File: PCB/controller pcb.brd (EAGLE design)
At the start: 84 x 86.5 mm, 43 parts, among them IC1 MAX481CSA, IC2 MAX481CSA, IC3 STM32F103C8T, U1 TPS62177.DQC, X2 2510-, X4 NC3FAH2, X5 NC3FAH2-0, X7 MINI-USB_4P-85-32004-40X

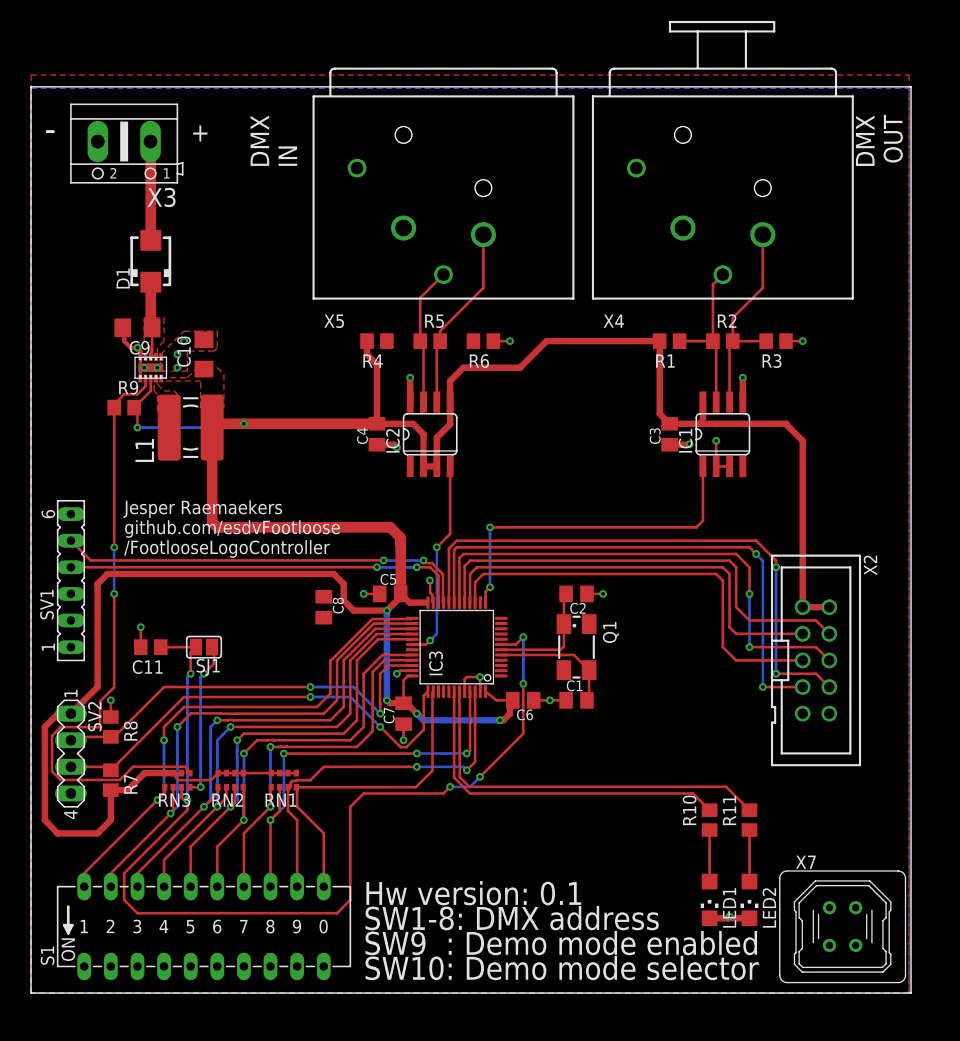
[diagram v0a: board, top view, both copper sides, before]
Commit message: Minor changes to fron PCB. changed positioning of segments and buttons
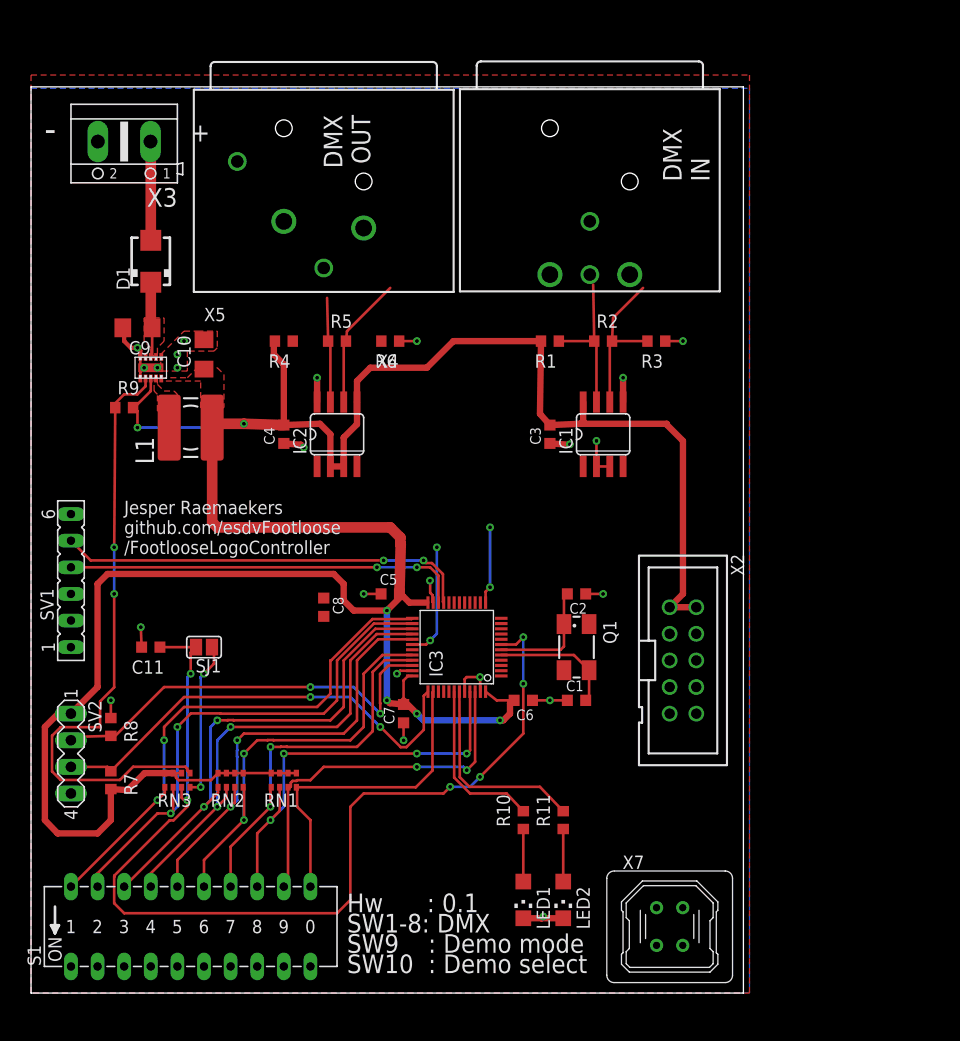
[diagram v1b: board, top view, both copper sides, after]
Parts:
- C1, C2, C3, C4, C5, C6, C7, C8: device rcl:C0805K -> rcl:C0603K
- C11: device rcl:C0805 -> rcl:C0603K
- R1, R10, R11, R2, R3, R4, R5, R6, R7, R8, R9: device rcl:R0805 -> rcl:R0603
- X4: value NC3FAH2 -> NC3MBH; device con-neutrik_ag:NC3FAH2 -> con-neutrik_ag:NC3MBH
- moved LED2 17.8 mm to (50.8, 8.89)
- moved R11 17.8 mm to (50.8, 16.5)
- moved LED1 17.8 mm to (47.0, 8.89)
- moved R10 17.8 mm to (47.0, 16.5)
- moved X7 16.5 mm to (61.0, 6.35)
- moved X4 13.3 mm to (53.3, 68.6)
- moved X2 12.7 mm to (62.2, 31.8)
- moved X5 11.4 mm to (27.9, 73.0)
- moved IC1 11.4 mm to (54.6, 53.3)
- moved R2 11.4 mm to (54.6, 62.2)
- moved R3 11.4 mm to (59.7, 62.2)
- moved C3 11.4 mm to (49.5, 53.3)
- moved R1 11.4 mm to (49.5, 62.2)
- moved C4 8.89 mm to (24.1, 53.3)
- moved R4 8.89 mm to (24.1, 62.2)
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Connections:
- removed net FP_CS1: IC3.18, X2.6
- removed net FP_CS2: IC3.19, X2.7
- removed net FP_CS3: IC3.20, X2.8
- removed net FP_MISO: IC3.16, X2.3
- removed net FP_MOSI: IC3.17, X2.4
- removed net FP_SCK: IC3.15, X2.5
- removed net VDDA: IC3.9
- removed net VSSA: IC3.8
- new net FP_!RESET: X2.5
- new net FP_SCL: X2.4
- new net FP_SDA: X2.3
- new net FP_SYNC: X2.6
- new net FP_TOUCH1: X2.7
- new net FP_TOUCH2: X2.8
- net +3V3: now also C8.1, IC3.9
- net GND: now also C8.2, IC3.8, X4.2; no longer X4.1
- net N$6: now also X4.1; no longer X4.2
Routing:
- net FP_CS3: track 53.9 -> 0.00 mm, vias 2 -> 0
- net FP_CS2: track 51.0 -> 0.00 mm, vias 2 -> 0
- net FP_CS1: track 48.4 -> 0.00 mm, vias 2 -> 0
- net FP_MOSI: track 43.6 -> 0.00 mm
- net FP_SCK: track 40.7 -> 0.00 mm
- net FP_MISO: track 40.4 -> 0.00 mm
- net DMX_IN: track 33.1 -> 7.36 mm
- net N$12: track 37.1 -> 19.4 mm
- net N$13: track 33.9 -> 16.2 mm
- net +3V3: track 274.7 -> 265.0 mm
- net DMX_OUT: track 19.3 -> 11.1 mm
- net N$7: track 17.8 -> 12.7 mm
- net N$6: track 20.5 -> 15.5 mm
- net N$8: track 13.2 -> 10.0 mm
- net !RST: track 94.5 -> 96.3 mm
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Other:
- board size 84 x 86.5 mm -> 68 x 86.5 mm
- board text added: "Hw : 0.1 SW1-8: DMX SW9 : Demo mode SW10 : Demo select"
- board text removed: "Hw version: 0.1 SW1-8: DMX address SW9 : Demo mode enabled SW10: Demo mode selector"

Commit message: pending changes...
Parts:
- added C12: (no value), rcl:C0603K
- added IC4: MAX481CSA, maxim:SO08
- added R12, R13, R14: (no value), rcl:R0603
- added X1: NC3FAH2-0, con-neutrik_ag:NC3FAH2-0
- moved X5 64.9 mm to (53.3, 13.3), turned to 180 degrees
- moved R4 50.3 mm to (61.0, 27.9), turned to 90 degrees
- moved R5 49.1 mm to (61.0, 24.8), turned to 270 degrees
- moved R6 48.6 mm to (61.0, 21.6), turned to 90 degrees
- moved C4 44.0 mm to (54.0, 21.0), turned to 0 degrees
- moved IC2 37.8 mm to (54.0, 24.8), turned to 270 degrees
- moved X7 27.4 mm to (80.6, 25.4)
- moved LED1 13.7 mm to (34.3, 3.81)
- moved LED2 13.7 mm to (38.1, 3.81)
- moved R10 12.8 mm to (34.3, 15.2)
- moved R11 12.8 mm to (38.1, 15.2)
- moved X2 8.28 mm to (61.6, 40.0)
- moved C1 2.84 mm to (53.3, 30.5)
- moved C2 2.84 mm to (53.3, 40.6)
- moved C5 2.84 mm to (35.6, 40.6)
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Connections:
- new net N$11: IC4.7, R12.1, R13.1, X1.3
- new net N$2: IC4.6, R13.2, R14.2, X1.2
- net +3V3: now also C12.1, IC1.5, IC4.2, IC4.3, IC4.5, R12.2; no longer IC1.8
- net DMX_IN: now also IC4.4
- net GND: now also C12.2, IC1.8, IC4.8, R14.1, X1.1, X1.G; no longer IC1.5
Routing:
- net +3V3: track 265.0 -> 305.1 mm, vias 6 -> 8
- net DMX_IN: track 7.36 -> 37.8 mm, vias 2 -> 0
- net N$2: track 0.00 -> 21.5 mm
- net N$7: track 12.7 -> 30.1 mm
- net N$11: track 0.00 -> 17.3 mm
- net DMX_OUT: track 11.1 -> 27.5 mm
- net GND: track 46.0 -> 30.1 mm, vias 23 -> 17
- net N$8: track 10.0 -> 24.5 mm
- net !RST: track 96.3 -> 105.9 mm
- net SWCLK: track 43.3 -> 51.5 mm
- net SWDIO: track 39.9 -> 47.3 mm
- net DIPSW1: track 50.3 -> 57.3 mm
- net N$14: track 15.0 -> 21.9 mm
- net DIPSW5: track 42.4 -> 48.2 mm
- net DIPSW3: track 46.8 -> 52.4 mm
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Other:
- board text added: "1-9: DMX 10 : Test"
- board text removed: "Hw : 0.1 SW1-8: DMX SW9 : Demo mode SW10 : Demo select"

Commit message: Updated to STM32f303
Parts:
- removed IC3: STM32F103C8T, micro-stm:LQFP48
- removed X7: MINI-USB_4P-85-32004-40X, con-cypressindustries:85-32004-40X
- added U$1: STM32F303CCLQFP48, comp:LQFP48
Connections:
- removed net FP_!RESET: X2.5
- removed net N$15: IC3.39
- removed net VBAT: IC3.1
- net !RST: now also U$1.7, X2.5; no longer IC3.7
- net +3V3: now also U$1.24, U$1.36, U$1.48, U$1.9; no longer IC3.24, IC3.36, IC3.48, IC3.9
- net DEBUG_RX: now also U$1.22; no longer IC3.22
- net DEBUG_TX: now also U$1.21; no longer IC3.21
- net DIPSW1: now also U$1.25; no longer IC3.25
- net DIPSW10: now also U$1.38; no longer IC3.38
- net DIPSW2: now also U$1.26; no longer IC3.26
- net DIPSW3: now also U$1.27; no longer IC3.27
- net DIPSW4: now also U$1.28; no longer IC3.28
- net DIPSW5: now also U$1.29; no longer IC3.29
- net DIPSW6: now also U$1.32; no longer IC3.32
- net DIPSW7: now also U$1.33; no longer IC3.33
- net DIPSW8: now also U$1.45; no longer IC3.45
- net DIPSW9: now also U$1.46; no longer IC3.46
- net DMX_IN: now also U$1.13; no longer IC3.13
- net DMX_OUT: now also U$1.30; no longer IC3.30
- net FP_SCL: now also U$1.42
- net FP_SDA: now also U$1.43
- net FP_SYNC: now also U$1.10
- net FP_TOUCH1: now also U$1.11
- net FP_TOUCH2: now also U$1.12
- net GND: now also U$1.23, U$1.35, U$1.47, U$1.8; no longer IC3.23, IC3.35, IC3.44, IC3.47, IC3.8
- net N$12: now also U$1.41; no longer IC3.43
- net N$13: now also U$1.40; no longer IC3.42
- net N$4: now also U$1.6; no longer IC3.6
- net N$5: now also U$1.5; no longer IC3.5
- net SWCLK: now also U$1.37; no longer IC3.37
- net SWDIO: now also U$1.34; no longer IC3.34
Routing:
- net FP_SCL: track 0.00 -> 34.0 mm, vias 0 -> 3
- net FP_SDA: track 0.00 -> 31.0 mm, vias 0 -> 3
- net FP_SYNC: track 0.00 -> 27.9 mm
- net FP_TOUCH2: track 0.00 -> 25.3 mm
- net !RST: track 105.9 -> 129.0 mm, vias 6 -> 7
- net FP_TOUCH1: track 0.00 -> 22.3 mm
- net +3V3: track 305.1 -> 312.1 mm
- net DMX_IN: track 37.8 -> 31.2 mm
- net N$8: track 24.5 -> 25.9 mm
- net N$7: track 30.1 -> 31.6 mm
- net GND: track 30.1 -> 29.8 mm, vias 17 -> 18

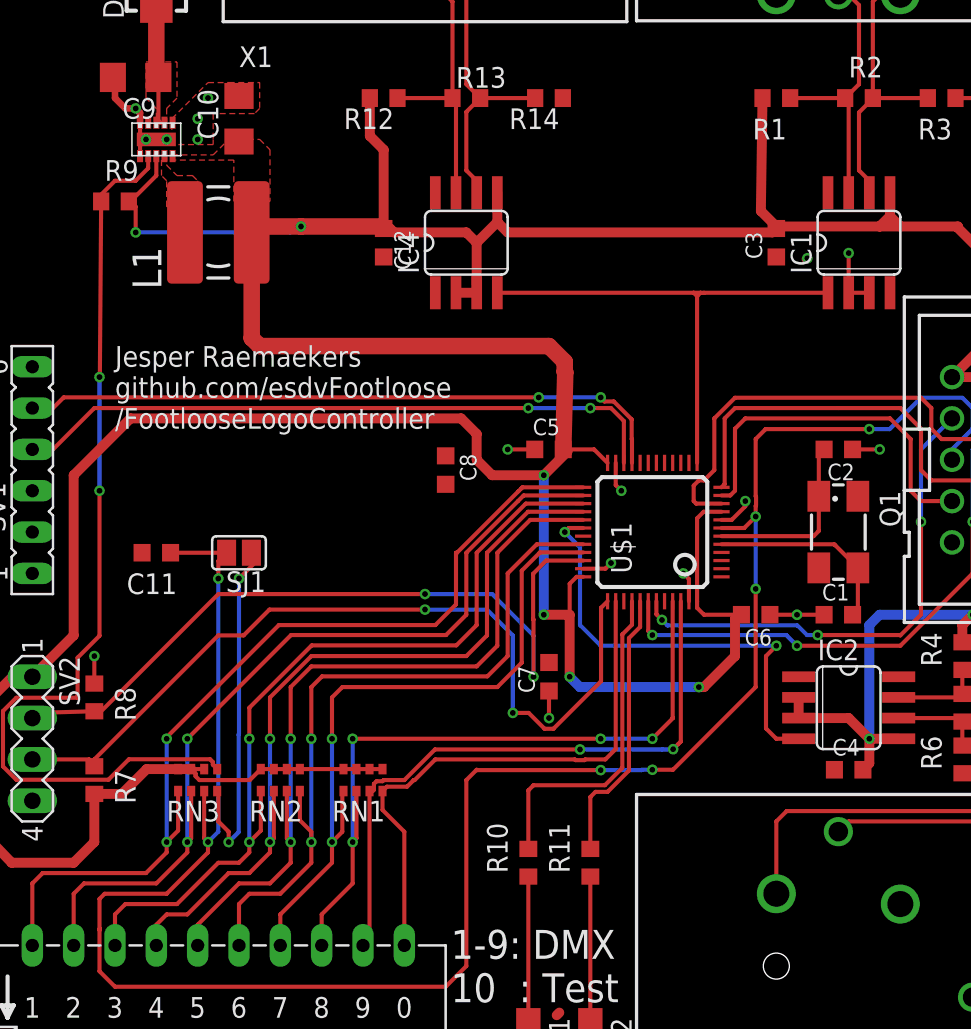
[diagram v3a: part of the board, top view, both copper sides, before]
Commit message: Placed extra decoupling cap and cleaned up some routing
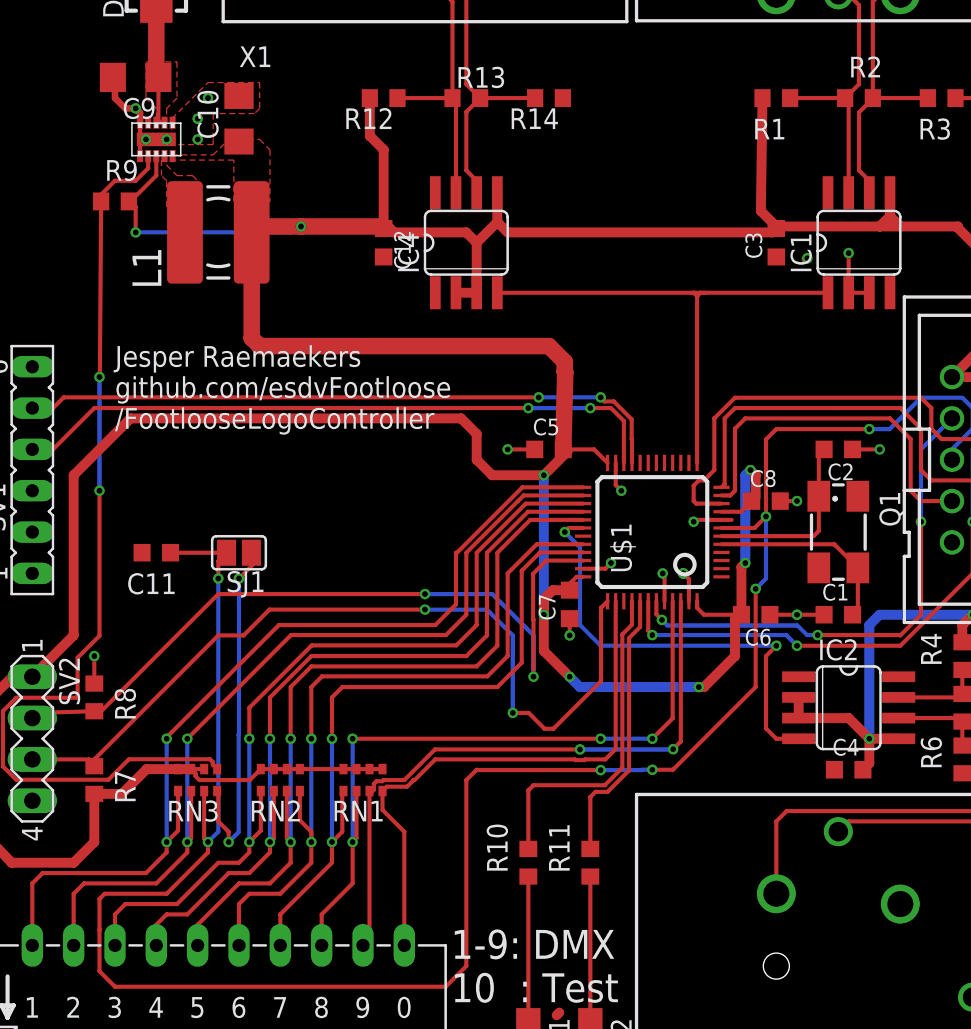
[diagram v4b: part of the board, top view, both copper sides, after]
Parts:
- moved C8 19.8 mm to (48.9, 37.5), turned to 0 degrees
- moved C7 4.62 mm to (36.8, 31.1)
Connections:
- net GND: now also IC1.4, U$1.44
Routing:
- net +3V3: track 312.1 -> 319.6 mm, vias 8 -> 10
- net GND: track 29.8 -> 32.2 mm, vias 18 -> 21

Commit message: Finalized PCBs
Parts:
- removed L1: (no value), rcl:POWER-CHOKE_WE-TPC
- added L2: LPS4018, inductor-coilcraft:LPS4018
- C10: value (none) -> 22u
- C9: value (none) -> 2.2uF
- R9: value (none) -> 100K
- moved C10 0.64 mm to (15.9, 61.0)
- renumbered SV2 to PROG, U$1 to IC3, U1 to IC5
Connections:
- net +3V3: now also L2.2; no longer L1.2
- net SW: now also L2.1; no longer L1.1
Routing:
- net GND: track 32.2 -> 27.7 mm, vias 21 -> 149
- net +3V3: track 319.6 -> 322.7 mm
- net DMX_IN: track 31.2 -> 33.4 mm

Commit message: fixed pinout on pcb, added test effect
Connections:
- removed net N$11: IC4.7, R12.1, R13.1, X1.3
- removed net N$6: IC1.6, R2.2, R3.2, X4.1
- new net N$15: IC4.7, R12.1, R13.1, X1.2
- new net N$16: IC1.6, R2.2, R3.2, X4.2
- net GND: now also X4.1; no longer X4.2
- net N$2: now also X1.3; no longer X1.2
- net N$7: now also X5.3; no longer X5.2
- net N$8: now also X5.2; no longer X5.3
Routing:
- net N$6: track 17.6 -> 0.00 mm
- net N$11: track 17.3 -> 0.00 mm
- net N$15: track 0.00 -> 16.7 mm
- net N$16: track 0.00 -> 16.3 mm
- net N$7: track 31.6 -> 27.1 mm
- net N$2: track 21.5 -> 19.7 mm
- net N$8: track 25.9 -> 25.0 mm
- net N$3: track 16.9 -> 16.2 mm
